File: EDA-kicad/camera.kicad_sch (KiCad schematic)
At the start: 3 parts, among them U6 FPC15pin-1mm-pitch-F52Q-1A7H1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

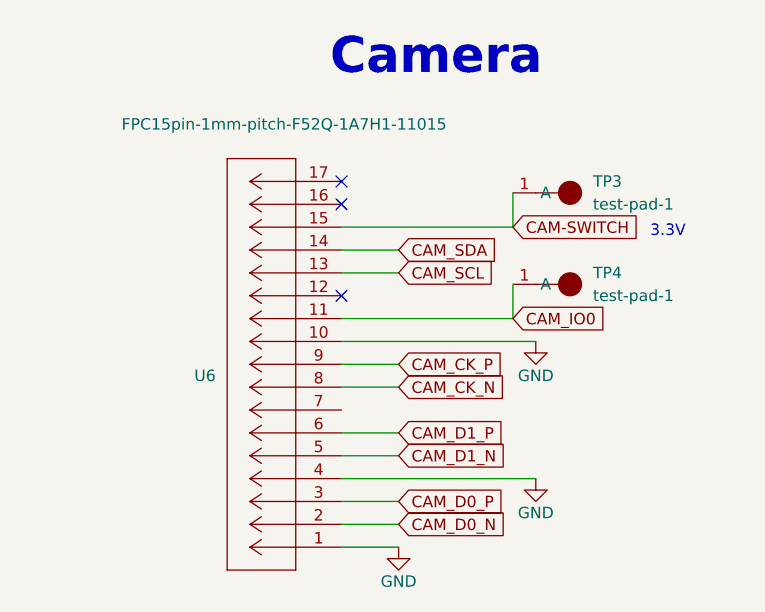
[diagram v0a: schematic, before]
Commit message: reannotate entire schematic
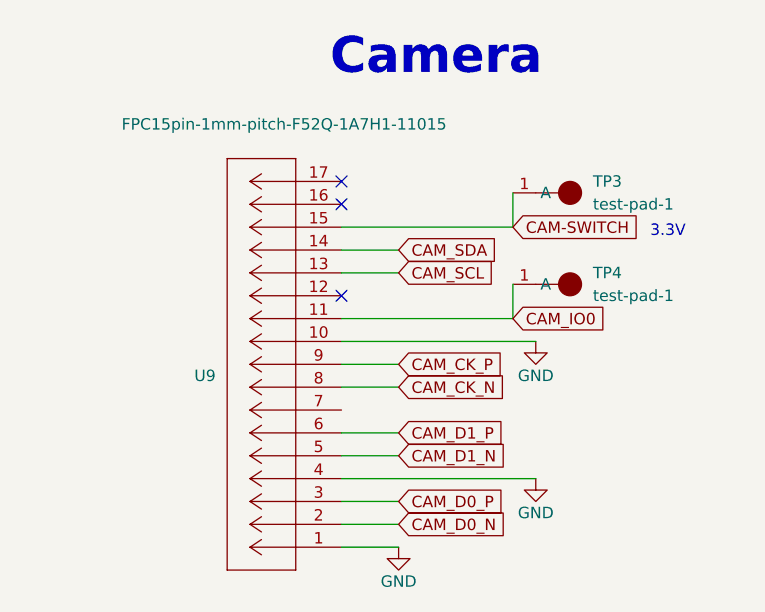
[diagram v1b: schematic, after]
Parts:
- renumbered U6 to U9
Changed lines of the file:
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@@
 		(on_board yes)
 		(dnp no)
-		(property "Reference" "#PWR023"
+		(property "Reference" "#PWR0126"
 			(at 151.13 93.98 0)
 			(effects
@@
 			(project "cm5-carrier"
 				(path "/28c5e4fe-1ec7-4477-97f0-d2ec1401fad5/7ec223ba-5b63-4970-8f4e-9b03f0ec9947"
-					(reference "#PWR023")
+					(reference "#PWR0126")
 					(unit 1)
 				)
@@
 		(on_board yes)
 		(dnp no)
-		(property "Reference" "#PWR015"
+		(property "Reference" "#PWR0128"
 			(at 135.89 116.84 0)
 			(effects
@@
 			(project "cm5-carrier"
 				(path "/28c5e4fe-1ec7-4477-97f0-d2ec1401fad5/7ec223ba-5b63-4970-8f4e-9b03f0ec9947"
-					(reference "#PWR015")
+					(reference "#PWR0128")
 					(unit 1)
 				)
@@
 		(on_board yes)
 		(dnp no)
-		(property "Reference" "#PWR024"
+		(property "Reference" "#PWR0127"
 			(at 151.13 109.22 0)
 			(effects
@@
 			(project "cm5-carrier"
 				(path "/28c5e4fe-1ec7-4477-97f0-d2ec1401fad5/7ec223ba-5b63-4970-8f4e-9b03f0ec9947"
-					(reference "#PWR024")
+					(reference "#PWR0127")
 					(unit 1)
 				)
@@
 		(on_board yes)
 		(dnp no)
-		(property "Reference" "U6"
+		(property "Reference" "U9"
 			(at 115.57 91.4401 0)
 			(effects
@@
 			(project "cm5-carrier"
 				(path "/28c5e4fe-1ec7-4477-97f0-d2ec1401fad5/7ec223ba-5b63-4970-8f4e-9b03f0ec9947"
-					(reference "U6")
-					(unit 1)
-				)
+					(reference "U9")
+					(unit 1)
+				)

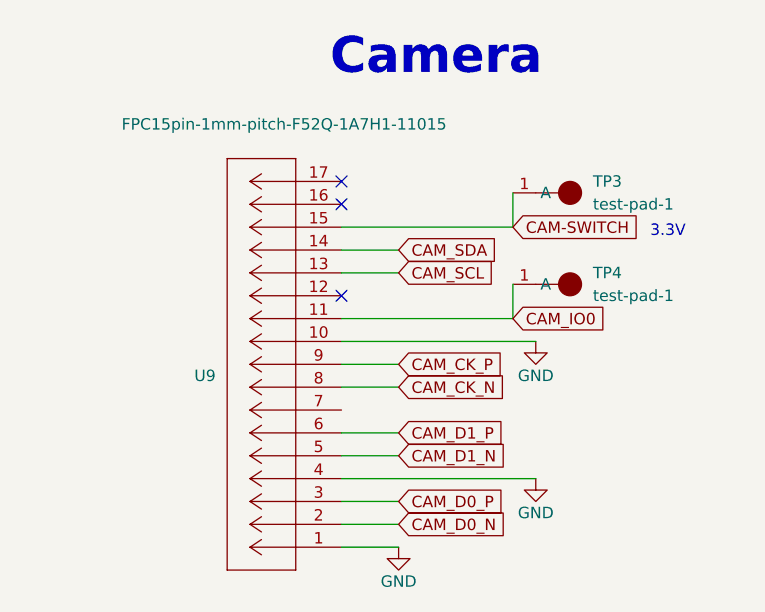
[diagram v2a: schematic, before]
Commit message: set everything except from power to DNP
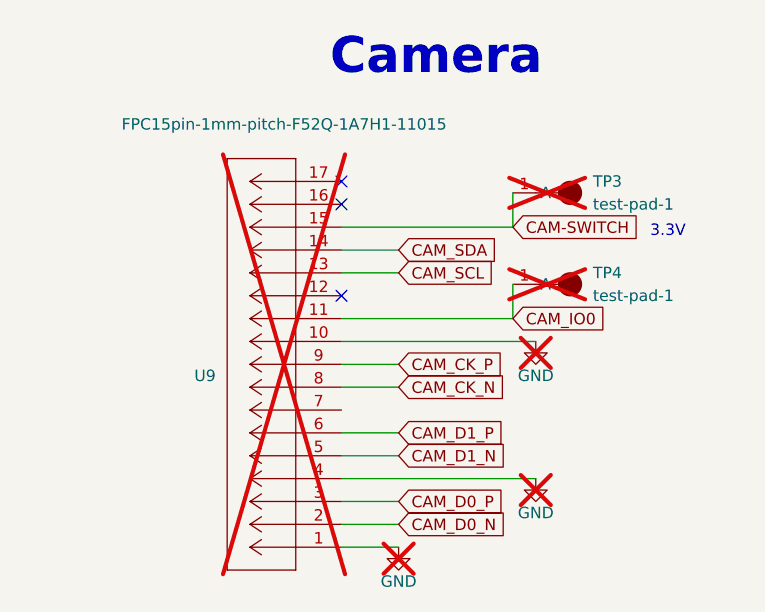
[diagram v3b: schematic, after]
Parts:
- TP3, TP4, U9: now not fitted

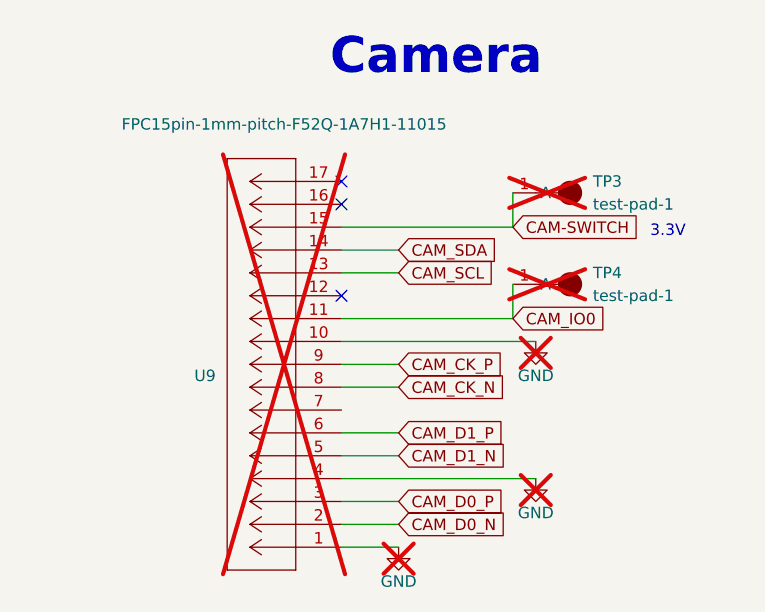
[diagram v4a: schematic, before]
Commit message: Improve KiCAD schematic design and labeling
- Replace overused global labels with hierarchical and local labels
- Add proper GND connections to components
- Fix BACKLIGHT- net issues
- Apply minor schematic fixes and cleanups
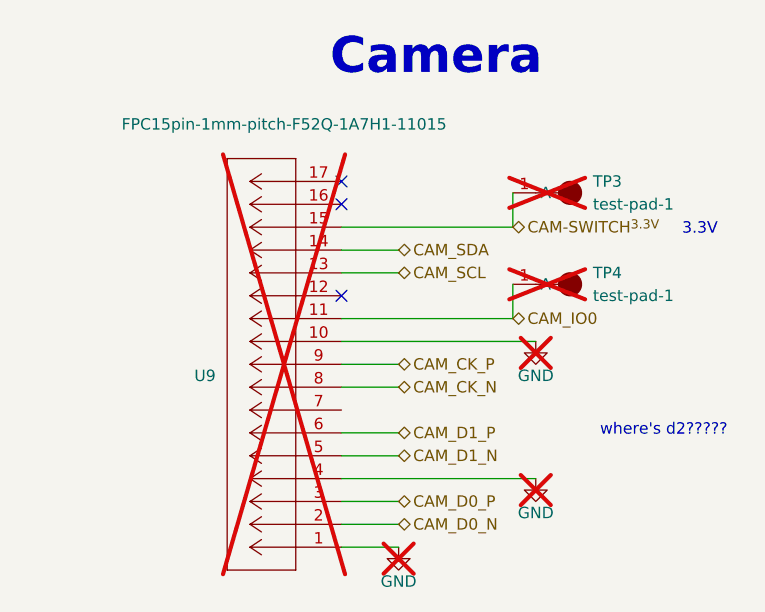
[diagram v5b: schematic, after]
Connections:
- net CAM-SWITCH renamed CAM-SWITCH^{3.3V}
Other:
- note added: "where's d2?????"
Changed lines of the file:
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@@
+		)
+	)
+	(text "where's d2?????"
+		(exclude_from_sim no)
+		(at 165.354 97.536 0)
+		(effects
+			(font
+				(size 1.27 1.27)
+			)
 		)
 	)
 	(text "3.3V"
 		(exclude_from_sim no)
-		(at 163.83 76.2 0)
+		(at 167.386 75.946 0)
 		(effects
 			(font
@@
 		)
 	)
-	(global_label "CAM_SDA"
-		(shape input)
+	(hierarchical_label "CAM_SDA"
+		(shape bidirectional)
 		(at 135.89 77.47 0)
-		(fields_autoplaced yes)
-		(effects
-			(font
-				(size 1.27 1.27)
-			)
-			(justify left)
-		)
-		(property "Intersheetrefs" "${INTERSHEET_REFS}"
-			(at 146.6488 77.3906 0)
-			(effects
-				(font
-					(size 1.27 1.27)
-				)
-				(justify left)
-				(hide yes)
-			)
-		)
-	)
-	(global_label "CAM_CK_N"
-		(shape input)
+		(effects
+			(font
+				(size 1.27 1.27)
+			)
+			(justify left)
+		)
+	)
+	(hierarchical_label "CAM-SWITCH^{3.3V}"
+		(shape bidirectional)
+		(at 148.59 74.93 0)
+		(effects
+			(font
+				(size 1.27 1.27)
+			)
+			(justify left)
+		)
+	)
+	(hierarchical_label "CAM_SCL"
+		(shape bidirectional)
+		(at 135.89 80.01 0)
+		(effects
+			(font
+				(size 1.27 1.27)
+			)
+			(justify left)
+		)
+	)
+	(hierarchical_label "CAM_D1_N"
+		(shape bidirectional)
+		(at 135.89 100.33 0)
+		(effects
+			(font
+				(size 1.27 1.27)
+			)
+			(justify left)
+		)
+	)
+	(hierarchical_label "CAM_IO0"
+		(shape bidirectional)
+		(at 148.59 85.09 0)
+		(effects
+			(font
+				(size 1.27 1.27)
+			)
+			(justify left)
+		)
+	)
+	(hierarchical_label "CAM_D0_P"
+		(shape bidirectional)
+		(at 135.89 105.41 0)
+		(effects
+			(font
+				(size 1.27 1.27)
+			)
+			(justify left)
+		)
+	)
+	(hierarchical_label "CAM_CK_P"
+		(shape bidirectional)
+		(at 135.89 90.17 0)
+		(effects
+			(font
+				(size 1.27 1.27)
+			)
+			(justify left)
+		)
+	)
+	(hierarchical_label "CAM_CK_N"
+		(shape bidirectional)
 		(at 135.89 92.71 0)
-		(fields_autoplaced yes)
-		(effects
-			(font
-				(size 1.27 1.27)
-			)
-			(justify left)
-		)
-		(property "Intersheetrefs" "${INTERSHEET_REFS}"
-			(at 147.9188 92.6306 0)
-			(effects
-				(font
-					(size 1.27 1.27)
-				)
-				(justify left)
-				(hide yes)
-			)
-		)
-	)
-	(global_label "CAM_CK_P"
-		(shape input)
-		(at 135.89 90.17 0)
-		(fields_autoplaced yes)
-		(effects
-			(font
-				(size 1.27 1.27)
-			)
-			(justify left)
-		)
-		(property "Intersheetrefs" "${INTERSHEET_REFS}"
-			(at 147.8583 90.0906 0)
-			(effects
-				(font
-					(size 1.27 1.27)
-				)
-				(justify left)
-				(hide yes)
-			)
-		)
-	)
-	(global_label "CAM_D1_N"
-		(shape input)
-		(at 135.89 100.33 0)
-		(fields_autoplaced yes)
-		(effects
-			(font
-				(size 1.27 1.27)
-			)
-			(justify left)
-		)
-		(property "Intersheetrefs" "${INTERSHEET_REFS}"
-			(at 147.8583 100.2506 0)
-			(effects
-				(font
-					(size 1.27 1.27)
-				)
-				(justify left)
-				(hide yes)
-			)
-		)
-	)
-	(global_label "CAM_D0_P"
-		(shape input)
-		(at 135.89 105.41 0)
-		(fields_autoplaced yes)
-		(effects
-			(font
-				(size 1.27 1.27)
-			)
-			(justify left)
-		)
-		(property "Intersheetrefs" "${INTERSHEET_REFS}"
-			(at 147.7979 105.3306 0)
-			(effects
-				(font
-					(size 1.27 1.27)
-				)
-				(justify left)
-				(hide yes)
-			)
-		)
-	)
-	(global_label "CAM_IO0"
-		(shape input)
-		(at 148.59 85.09 0)
-		(fields_autoplaced yes)
-		(effects
-			(font
-				(size 1.27 1.27)
-			)
-			(justify left)
-		)
-		(property "Intersheetrefs" "${INTERSHEET_REFS}"
-			(at 158.9255 85.0106 0)
-			(effects
-				(font
-					(size 1.27 1.27)
-				)
-				(justify left)
-				(hide yes)
-			)
-		)
-	)
-	(global_label "CAM-SWITCH"
-		(shape input)
-		(at 148.59 74.93 0)
-		(fields_autoplaced yes)
-		(effects
-			(font
-				(size 1.27 1.27)
-			)
-			(justify left)
-		)
-		(property "Intersheetrefs" "${INTERSHEET_REFS}"
-			(at 163.2193 74.8506 0)
-			(effects
-				(font
-					(size 1.27 1.27)
-				)
-				(justify left)
-				(hide yes)
-			)
-		)
-	)
-	(global_label "CAM_D0_N"
-		(shape input)
+		(effects
+			(font
+				(size 1.27 1.27)
+			)
+			(justify left)
+		)
+	)
+	(hierarchical_label "CAM_D0_N"
+		(shape bidirectional)
 		(at 135.89 107.95 0)
-		(fields_autoplaced yes)
-		(effects
-			(font
-				(size 1.27 1.27)
-			)
-			(justify left)
-		)
-		(property "Intersheetrefs" "${INTERSHEET_REFS}"
-			(at 147.8583 107.8706 0)
-			(effects
-				(font
-					(size 1.27 1.27)
-				)
-				(justify left)
-				(hide yes)
-			)
-		)
-	)
-	(global_label "CAM_SCL"
-		(shape input)
-		(at 135.89 80.01 0)
-		(fields_autoplaced yes)
-		(effects
-			(font
-				(size 1.27 1.27)
-			)
-			(justify left)
-		)
-		(property "Intersheetrefs" "${INTERSHEET_REFS}"
-			(at 146.5883 79.9306 0)
-			(effects
-				(font
-					(size 1.27 1.27)
-				)
-				(justify left)
-				(hide yes)
-			)
-		)
-	)
-	(global_label "CAM_D1_P"
-		(shape input)
+		(effects
+			(font
+				(size 1.27 1.27)
+			)
+			(justify left)
+		)
+	)
+	(hierarchical_label "CAM_D1_P"
+		(shape bidirectional)
 		(at 135.89 97.79 0)
-		(fields_autoplaced yes)
-		(effects
-			(font
-				(size 1.27 1.27)
-			)
-			(justify left)
-		)
-		(property "Intersheetrefs" "${INTERSHEET_REFS}"
-			(at 147.7979 97.7106 0)
-			(effects
-				(font
-					(size 1.27 1.27)
-				)
-				(justify left)
-				(hide yes)
-			)
-		)
-	)
+		(effects
+			(font
+				(size 1.27 1.27)
+			)
+			(justify left)
+		)
+	)
